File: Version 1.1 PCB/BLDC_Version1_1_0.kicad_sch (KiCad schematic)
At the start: 17 parts, among them CN1 DB910-7.62-3P, SW1 SW_MEC_5E, SW2 SW_MEC_5E, U1 ESP32-S3-WROOM-1

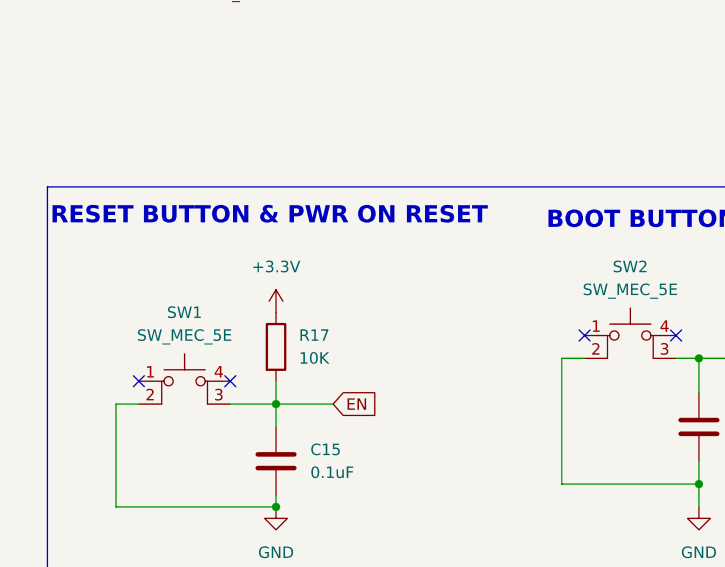
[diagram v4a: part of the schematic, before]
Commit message: Added silkscreen texts and logo
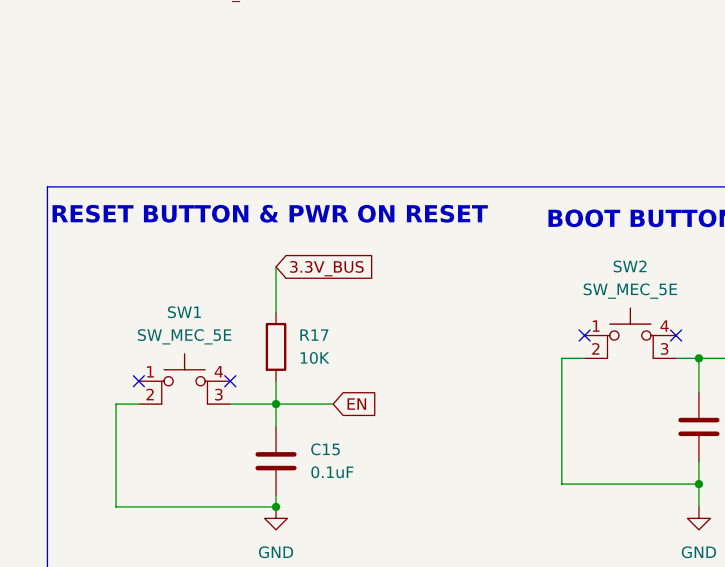
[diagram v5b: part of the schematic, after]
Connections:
- net +3.3V is gone; now on net 3.3V_BUS: R17.1
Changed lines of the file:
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@@
+	(wire
+		(pts
+			(xy 40.64 123.19) (xy 40.64 128.27)
+		)
+		(stroke
+			(width 0)
+			(type default)
+		)
+	)
 	(wire
 		(pts
@@
 		)
 	)
+	(global_label "3.3V_BUS"
+		(shape input)
+		(at 40.64 123.19 0)
+		(fields_autoplaced yes)
+		(effects
+			(font
+				(size 1.27 1.27)
+			)
+			(justify left)
+		)
+		(property "Intersheetrefs" "${INTERSHEET_REFS}"
+			(at 52.5152 123.19 0)
+			(effects
+				(font
+					(size 1.27 1.27)
+				)
+				(justify left)
+				(hide yes)
+			)
+		)
+	)
 	(global_label "16.8V_BUS"
 		(shape input)
@@
 			)
 		)
-	)
-	(symbol
-		(lib_id "power:+3.3V")
-		(at 40.64 128.27 0)
-		(unit 1)
-		(exclude_from_sim no)
-		(in_bom yes)
-		(on_board yes)
-		(dnp no)
-		(fields_autoplaced yes)
-		(property "Reference" "#PWR038"
-			(at 40.64 132.08 0)
-			(effects
-				(font
-					(size 1.27 1.27)
-				)
-				(hide yes)
-			)
-		)
-		(property "Value" "+3.3V"
-			(at 40.64 123.19 0)
-			(effects
-				(font
-					(size 1.27 1.27)
-				)
-			)
-		)
-		(property "Footprint" ""
-			(at 40.64 128.27 0)
-			(effects
-				(font
-					(size 1.27 1.27)
-				)
-				(hide yes)
-			)
-		)
-		(property "Datasheet" ""
-			(at 40.64 128.27 0)
-			(effects
-				(font
-					(size 1.27 1.27)
-				)
-				(hide yes)
-			)
-		)
-		(property "Description" "Power symbol creates a global label with name \"+3.3V\""
-			(at 40.64 128.27 0)
-			(effects
-				(font
-					(size 1.27 1.27)
-				)
-				(hide yes)
-			)
-		)
-		(pin "1"
-		)
-		(instances
-			(project "BLDC_Version1_1_0"
-				(path "/1ef2c161-9706-454e-ac1f-db9f896ae7e0"
-					(reference "#PWR038")
-					(unit 1)
-				)
-			)
-		)
